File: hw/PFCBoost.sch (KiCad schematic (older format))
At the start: 31 parts

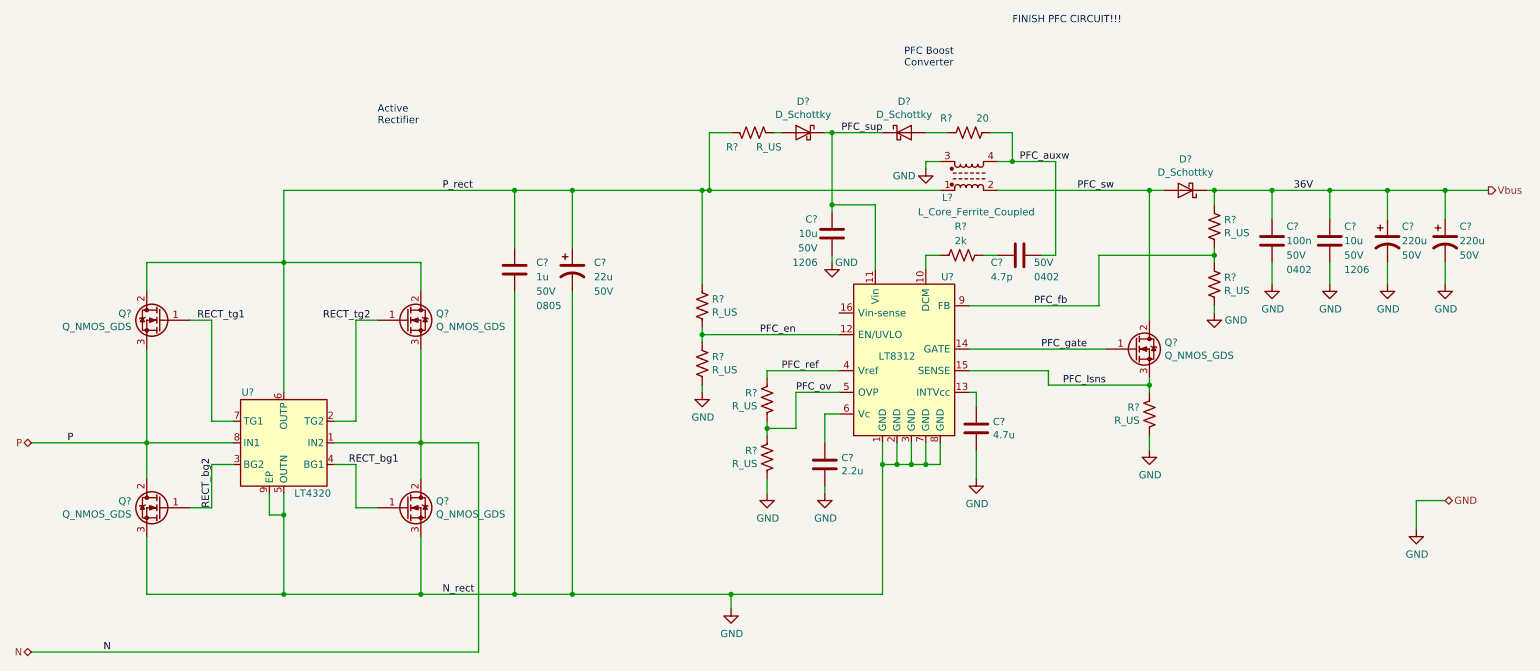
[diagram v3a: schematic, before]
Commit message: more component selection
more caps selected; updated primary switcher sim file
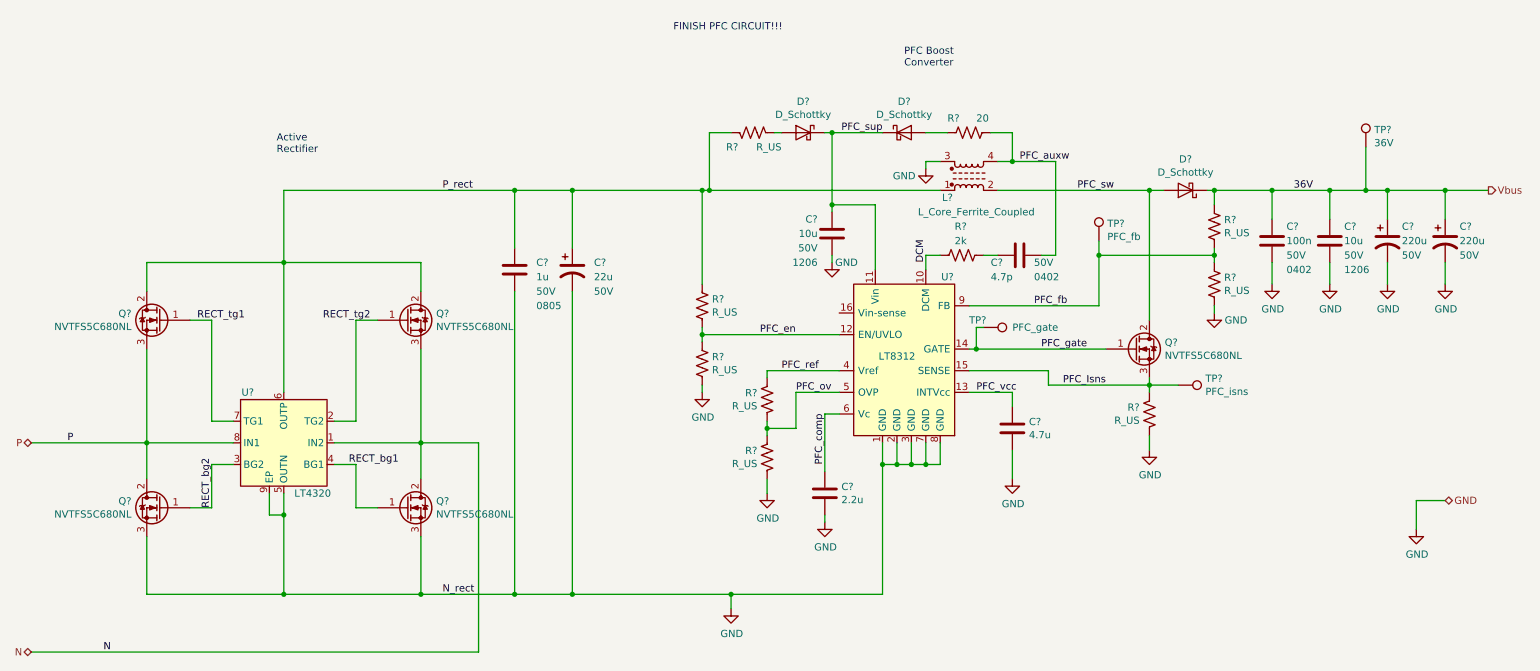
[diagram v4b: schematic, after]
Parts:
- removed Q? (x4): Q_NMOS_GDS, symbol Device:Q_NMOS_GDS
- added Q? (x4): NVTFS5C680NL, symbol Device:Q_NMOS_GDS
- added TP?: 36V, TestPoint:TestPoint_Keystone_5000-5004_Miniature, symbol Connector:TestPoint
- added TP?: PFC_fb, TestPoint:TestPoint_Keystone_5000-5004_Miniature, symbol Connector:TestPoint
- added TP?: PFC_isns, TestPoint:TestPoint_Keystone_5000-5004_Miniature, symbol Connector:TestPoint
- added TP?: PFC_gate, TestPoint:TestPoint_Keystone_5000-5004_Miniature, symbol Connector:TestPoint
- Q?: value Q_NMOS_GDS -> NVTFS5C680NL; MfrNum (none) -> OnSemi_NVTFS5C680NL
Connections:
- net GND: now also Q?.3 (S), Q?.3 (S)
- net N: now also Q?.2 (D), Q?.3 (S)
- net P: now also Q?.2 (D)
- net PFC_Isns: now also Q?.3 (S), TP?.1
- net PFC_fb: now also TP?.1
- net PFC_gate: now also Q?.1 (G), TP?.1
- net PFC_sw: now also Q?.2 (D)
- net P_rect: now also Q?.2 (D)
- net RECT_bg1: now also Q?.1 (G)
- net RECT_bg2: now also Q?.1 (G)
- net RECT_tg2: now also Q?.1 (G)
- net Vbus: now also TP?.1
- net DCM: now reaches R?.1, U?.10 (DCM)
- net PFC_vcc: now reaches C?.1, U?.13 (INTVcc)
- net PFC_comp: now reaches C?.1, U?.6 (Vc)
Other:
- moved on the sheet: C?
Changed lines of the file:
@@
 P 1700 2850
 F 0 "Q?" H 1906 2896 50  0000 L CNN
-F 1 "Q_NMOS_GDS" H 1906 2805 50  0000 L CNN
+F 1 "NVTFS5C680NL" H 1906 2805 50  0000 L CNN
 F 2 "" H 1900 2950 50  0001 C CNN
 F 3 "~" H 1700 2850 50  0001 C CNN
+F 4 "OnSemi_NVTFS5C680NL" H 1700 2850 50  0001 C CNN "MfrNum"
 	1    1700 2850
 	-1   0    0    -1
-$EndComp
-$Comp
-L Device:Q_NMOS_GDS Q?
-U 1 1 5E81228E
-P 1700 4150
-F 0 "Q?" H 1906 4196 50  0000 L CNN
-F 1 "Q_NMOS_GDS" H 1906 4105 50  0000 L CNN
-F 2 "" H 1900 4250 50  0001 C CNN
-F 3 "~" H 1700 4150 50  0001 C CNN
-	1    1700 4150
-	-1   0    0    -1
-$EndComp
-$Comp
-L Device:Q_NMOS_GDS Q?
-U 1 1 5E8122C2
-P 3400 4150
-F 0 "Q?" H 3605 4196 50  0000 L CNN
-F 1 "Q_NMOS_GDS" H 3605 4105 50  0000 L CNN
-F 2 "" H 3600 4250 50  0001 C CNN
-F 3 "~" H 3400 4150 50  0001 C CNN
-	1    3400 4150
-	1    0    0    -1
-$EndComp
-$Comp
-L Device:Q_NMOS_GDS Q?
-U 1 1 5E812393
-P 3400 2850
-F 0 "Q?" H 3605 2896 50  0000 L CNN
-F 1 "Q_NMOS_GDS" H 3605 2805 50  0000 L CNN
-F 2 "" H 3600 2950 50  0001 C CNN
-F 3 "~" H 3400 2850 50  0001 C CNN
-	1    3400 2850
-	1    0    0    -1
 $EndComp
 Wire Wire Line
@@
 L Device:C C?
 U 1 1 5E81BE4D
-P 7350 3600
-F 0 "C?" H 7465 3646 50  0000 L CNN
-F 1 "4.7u" H 7465 3555 50  0000 L CNN
-F 2 "Capacitor_SMD:C_0805_2012Metric_Pad1.15x1.40mm_HandSolder" H 7388 3450 50  0001 C CNN
-F 3 "~" H 7350 3600 50  0001 C CNN
-	1    7350 3600
-	1    0    0    -1
-$EndComp
-Wire Wire Line
-	7300 3350 7350 3350
-Wire Wire Line
-	7350 3350 7350 3450
+P 7600 3600
+F 0 "C?" H 7715 3646 50  0000 L CNN
+F 1 "4.7u" H 7715 3555 50  0000 L CNN
+F 2 "Capacitor_SMD:C_0805_2012Metric_Pad1.15x1.40mm_HandSolder" H 7638 3450 50  0001 C CNN
+F 3 "~" H 7600 3600 50  0001 C CNN
+	1    7600 3600
+	1    0    0    -1
+$EndComp
+Wire Wire Line
+	7300 3350 7600 3350
+Wire Wire Line
+	7600 3350 7600 3450
 Wire Wire Line
 	6400 3500 6300 3500
@@
 L power:GND #PWR?
 U 1 1 5E81DFB4
-P 6300 4050
-F 0 "#PWR?" H 6300 3800 50  0001 C CNN
-F 1 "GND" H 6305 3877 50  0000 C CNN
-F 2 "" H 6300 4050 50  0001 C CNN
-F 3 "" H 6300 4050 50  0001 C CNN
-	1    6300 4050
+P 6300 4250
+F 0 "#PWR?" H 6300 4000 50  0001 C CNN
+F 1 "GND" H 6305 4077 50  0000 C CNN
+F 2 "" H 6300 4250 50  0001 C CNN
+F 3 "" H 6300 4250 50  0001 C CNN
+	1    6300 4250
 	1    0    0    -1
 $EndComp
@@
 L power:GND #PWR?
 U 1 1 5E81DFD1
-P 7350 3950
-F 0 "#PWR?" H 7350 3700 50  0001 C CNN
-F 1 "GND" H 7355 3777 50  0000 C CNN
-F 2 "" H 7350 3950 50  0001 C CNN
-F 3 "" H 7350 3950 50  0001 C CNN
-	1    7350 3950
-	1    0    0    -1
-$EndComp
-Wire Wire Line
-	7350 3750 7350 3950
+P 7600 3950
+F 0 "#PWR?" H 7600 3700 50  0001 C CNN
+F 1 "GND" H 7605 3777 50  0000 C CNN
+F 2 "" H 7600 3950 50  0001 C CNN
+F 3 "" H 7600 3950 50  0001 C CNN
+	1    7600 3950
+	1    0    0    -1
+$EndComp
+Wire Wire Line
+	7600 3750 7600 3950
 $Comp
 L power:GND #PWR?
@@
 L Device:C C?
 U 1 1 5E829D2A
-P 6300 3850
-F 0 "C?" H 6415 3896 50  0000 L CNN
-F 1 "2.2u" H 6415 3805 50  0000 L CNN
-F 2 "Capacitor_SMD:C_0805_2012Metric_Pad1.15x1.40mm_HandSolder" H 6338 3700 50  0001 C CNN
-F 3 "~" H 6300 3850 50  0001 C CNN
-	1    6300 3850
-	1    0    0    -1
-$EndComp
-Wire Wire Line
-	6300 4000 6300 4050
+P 6300 4050
+F 0 "C?" H 6415 4096 50  0000 L CNN
+F 1 "2.2u" H 6415 4005 50  0000 L CNN
+F 2 "Capacitor_SMD:C_0805_2012Metric_Pad1.15x1.40mm_HandSolder" H 6338 3900 50  0001 C CNN
+F 3 "~" H 6300 4050 50  0001 C CNN
+	1    6300 4050
+	1    0    0    -1
+$EndComp
+Wire Wire Line
+	6300 4200 6300 4250
 Wire Wire Line
 	6100 3350 6400 3350
 Wire Wire Line
 	5900 3200 6400 3200
-Wire Wire Line
-	6300 3700 6300 3500
-$Comp
-L Device:Q_NMOS_GDS Q?
-U 1 1 5E8395C3
-P 8450 3050
-F 0 "Q?" H 8655 3096 50  0000 L CNN
-F 1 "Q_NMOS_GDS" H 8655 3005 50  0000 L CNN
-F 2 "" H 8650 3150 50  0001 C CNN
-F 3 "~" H 8450 3050 50  0001 C CNN
-	1    8450 3050
-	1    0    0    -1
-$EndComp
 $Comp
 L Device:R_US R?
@@
 	8550 3250 8550 3300
 Wire Wire Line
-	7300 3050 8250 3050
+	7300 3050 7350 3050
 Wire Wire Line
 	8550 3300 7850 3300
@@
 Text HLabel 10600 4100 2    50   BiDi ~ 0
 GND
-Text Notes 3200 1500 0    50   ~ 0
+Text Notes 2500 1700 0    50   ~ 0
 Active\nRectifier
 Text Notes 6850 1100 0    50   ~ 0
@@
 	2550 4750 3500 4750
 Connection ~ 5650 4750
-Text Notes 7600 800  0    50   ~ 0
+Text Notes 5250 850  0    50   ~ 0
 FINISH PFC CIRCUIT!!!
 $Comp
@@
 Wire Wire Line
 	9000 1950 9400 1950
-Wire Wire Line
-	9000 2350 9000 2400
 $Comp
 L power:GND #PWR?
@@
 	9000 2800 9000 2750
 Wire Wire Line
-	9000 2400 8200 2400
-Wire Wire Line
-	8200 2400 8200 2750
-Wire Wire Line
 	8200 2750 7300 2750
-Connection ~ 9000 2400
-Wire Wire Line
-	9000 2400 9000 2450
 $Comp
 L Device:R_US R?
@@
 U 1 1 5EC1B479
 P 7300 1550
-F 0 "R?" V 7400 1750 50  0000 R CNN
+F 0 "R?" V 7400 1700 50  0000 R CNN
 F 1 "20" V 7400 1500 50  0000 R CNN
 F 2 "Resistor_SMD:R_0603_1608Metric" V 7340 1540 50  0001 C CNN
@@
 Connection ~ 9800 1950
 Wire Wire Line
-	9800 1950 10200 1950
+	9800 1950 10050 1950
 Text Label 7750 2750 0    50   ~ 0
 PFC_fb
@@
 Text Label 8050 1950 0    50   ~ 0
 PFC_sw
+$Comp
+L Connector:TestPoint TP?
+U 1 1 5EB85070
+P 10050 1650
+AR Path="/5E80D1C0/5EB85070" Ref="TP?"  Part="1"
+AR Path="/5E80D210/5EB85070" Ref="TP?"  Part="1"
+F 0 "TP?" H 10108 1770 50  0000 L CNN
+F 1 "36V" H 10108 1679 50  0000 L CNN
+F 2 "TestPoint:TestPoint_Keystone_5000-5004_Miniature" H 10250 1650 50  0001 C CNN
+F 3 "~" H 10250 1650 50  0001 C CNN
+	1    10050 1650
+	1    0    0    -1
+$EndComp
+Wire Wire Line
+	10050 1650 10050 1950
+Connection ~ 10050 1950
+Wire Wire Line
+	10050 1950 10200 1950
+$Comp
+L Connector:TestPoint TP?
+U 1 1 5EB8D7D8
+P 8200 2300
+AR Path="/5E80D1C0/5EB8D7D8" Ref="TP?"  Part="1"
+AR Path="/5E80D210/5EB8D7D8" Ref="TP?"  Part="1"
+F 0 "TP?" H 8258 2420 50  0000 L CNN
+F 1 "PFC_fb" H 8258 2329 50  0000 L CNN
+F 2 "TestPoint:TestPoint_Keystone_5000-5004_Miniature" H 8400 2300 50  0001 C CNN
+F 3 "~" H 8400 2300 50  0001 C CNN
+	1    8200 2300
+	1    0    0    -1
+$EndComp
+Wire Wire Line
+	9000 2350 9000 2400
+Wire Wire Line
+	9000 2400 8200 2400
+Wire Wire Line
+	8200 2400 8200 2750
+Connection ~ 9000 2400
+Wire Wire Line
+	9000 2400 9000 2450
+Wire Wire Line
+	8200 2300 8200 2400
+Connection ~ 8200 2400
+$Comp
+L Device:Q_NMOS_GDS Q?
+U 1 1 5EB9A68C
+P 1700 4150
+F 0 "Q?" H 1906 4196 50  0000 L CNN
+F 1 "NVTFS5C680NL" H 1906 4105 50  0000 L CNN
+F 2 "" H 1900 4250 50  0001 C CNN
+F 3 "~" H 1700 4150 50  0001 C CNN
+F 4 "OnSemi_NVTFS5C680NL" H 1700 4150 50  0001 C CNN "MfrNum"
+	1    1700 4150
+	-1   0    0    -1
+$EndComp
+$Comp
+L Device:Q_NMOS_GDS Q?
+U 1 1 5EB9A769
+P 3400 4150
+F 0 "Q?" H 3606 4196 50  0000 L CNN
+F 1 "NVTFS5C680NL" H 3606 4105 50  0000 L CNN
+F 2 "" H 3600 4250 50  0001 C CNN
+F 3 "~" H 3400 4150 50  0001 C CNN
+F 4 "OnSemi_NVTFS5C680NL" H 3400 4150 50  0001 C CNN "MfrNum"
+	1    3400 4150
+	1    0    0    -1
+$EndComp
+$Comp
+L Device:Q_NMOS_GDS Q?
+U 1 1 5EB9ED28
+P 3400 2850
+F 0 "Q?" H 3606 2896 50  0000 L CNN
+F 1 "NVTFS5C680NL" H 3606 2805 50  0000 L CNN
+F 2 "" H 3600 2950 50  0001 C CNN
+F 3 "~" H 3400 2850 50  0001 C CNN
+F 4 "OnSemi_NVTFS5C680NL" H 3400 2850 50  0001 C CNN "MfrNum"
+	1    3400 2850
+	1    0    0    -1
+$EndComp
+Text Label 6300 3850 1    50   ~ 0
+PFC_comp
+Wire Wire Line
+	6300 3500 6300 3900
+Text Label 7350 3350 0    50   ~ 0
+PFC_vcc
+Text Label 7000 2450 1    50   ~ 0
+DCM
+$Comp
+L Device:Q_NMOS_GDS Q?
+U 1 1 5EBB0DF8
+P 8450 3050
+F 0 "Q?" H 8656 3096 50  0000 L CNN
+F 1 "NVTFS5C680NL" H 8656 3005 50  0000 L CNN
+F 2 "" H 8650 3150 50  0001 C CNN
+F 3 "~" H 8450 3050 50  0001 C CNN
+F 4 "OnSemi_NVTFS5C680NL" H 8450 3050 50  0001 C CNN "MfrNum"
+	1    8450 3050
+	1    0    0    -1
+$EndComp
+$Comp
+L Connector:TestPoint TP?
+U 1 1 5EBB112C
+P 8750 3300
+AR Path="/5E80D1C0/5EBB112C" Ref="TP?"  Part="1"
+AR Path="/5E80D210/5EBB112C" Ref="TP?"  Part="1"
+F 0 "TP?" V 8704 3488 50  0000 L CNN
+F 1 "PFC_isns" V 8795 3488 50  0000 L CNN
+F 2 "TestPoint:TestPoint_Keystone_5000-5004_Miniature" H 8950 3300 50  0001 C CNN
+F 3 "~" H 8950 3300 50  0001 C CNN
+	1    8750 3300
+	0    1    1    0
+$EndComp
+Wire Wire Line
+	8750 3300 8550 3300
+$Comp
+L Connector:TestPoint TP?
+U 1 1 5EBB59E8
+P 7400 2900
+AR Path="/5E80D1C0/5EBB59E8" Ref="TP?"  Part="1"
+AR Path="/5E80D210/5EBB59E8" Ref="TP?"  Part="1"
+F 0 "TP?" V 7350 2800 50  0000 L CNN
+F 1 "PFC_gate" V 7400 3100 50  0000 L CNN
+F 2 "TestPoint:TestPoint_Keystone_5000-5004_Miniature" H 7600 2900 50  0001 C CNN
+F 3 "~" H 7600 2900 50  0001 C CNN
+	1    7400 2900
+	0    1    1    0
+$EndComp
+Wire Wire Line
+	7400 2900 7350 2900
+Wire Wire Line
+	7350 2900 7350 3050
+Connection ~ 7350 3050
+Wire Wire Line
+	7350 3050 8250 3050
 $EndSCHEMATC
